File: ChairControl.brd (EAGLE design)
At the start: 150 x 84 mm, 28 parts, among them J1 Digital_0_7, J2 Analog, J3 Digital_8_13, SW1 SWITCH-DPDT3, X1 INPUT, X2 OUTPUT, X4 INPUT

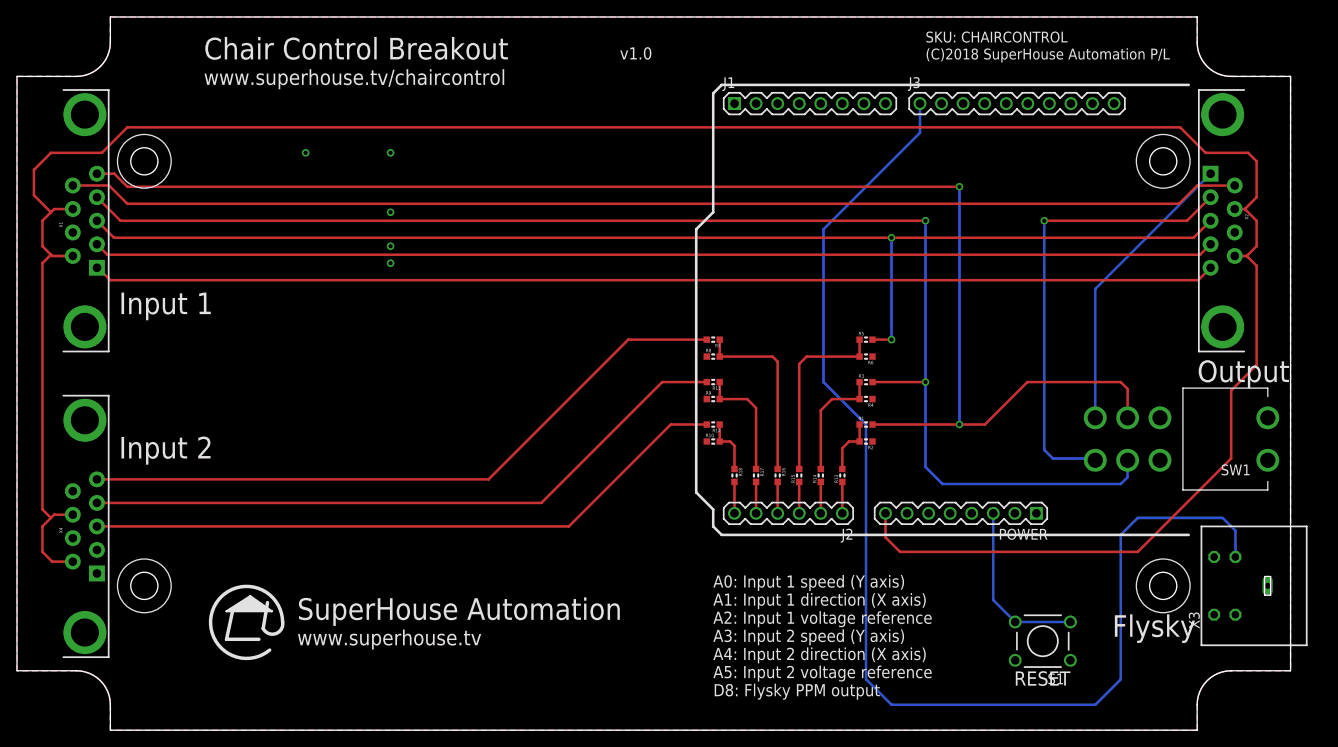
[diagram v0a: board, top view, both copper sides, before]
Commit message: Added trim inputs and extra headers for Mega footprint
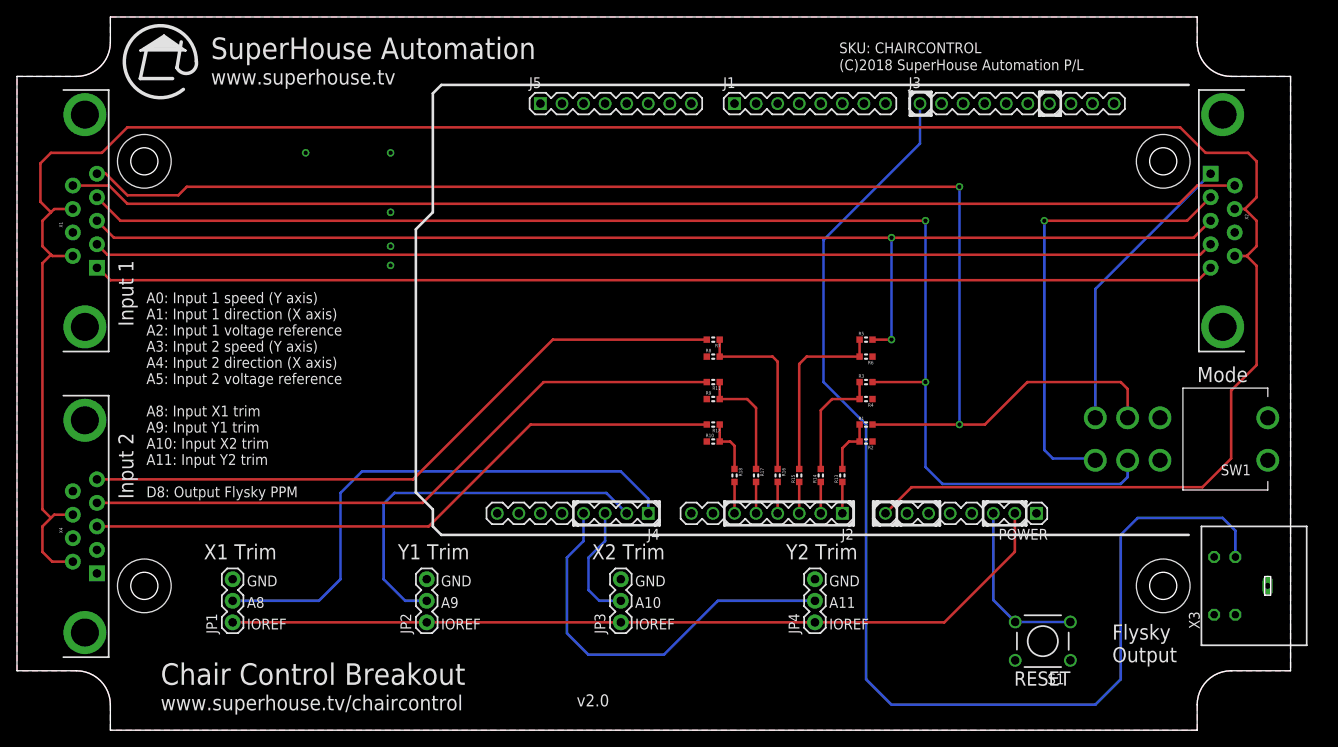
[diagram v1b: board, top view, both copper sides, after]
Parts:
- added J4: Analog, freetronics-jon:1X08
- added J5: Digital_0_7, freetronics:1X08
- added JP1, JP2, JP3, JP4: (no value), freetronics-jon:1X03
- J2: device freetronics:1X06 -> freetronics-jon:1X08
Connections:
- new net A10: J4.3, JP3.2
- new net A11: J4.4, JP4.2
- new net A8: J4.1, JP1.2
- new net A9: J4.2, JP2.2
- net GND: now also JP1.3, JP2.3, JP3.3, JP4.3
- net IOREF: now also JP1.1, JP2.1, JP3.1, JP4.1
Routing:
- net IOREF: track 0.00 -> 100.1 mm
- net A8: track 0.00 -> 64.3 mm
- net A11: track 0.00 -> 47.8 mm
- net A9: track 0.00 -> 45.2 mm
- net A10: track 0.00 -> 14.2 mm
- net 12V: track 297.6 -> 291.5 mm
- net SPEED_IN: track 166.1 -> 166.9 mm
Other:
- board text added: "A0: Input 1 speed (Y axis) A1: Input 1 direction (X axis) A2: Input 1 voltage reference A3: Input 2 speed (Y axis) A4: Input 2 direction (X axis) A5: Input 2 voltage reference A8: Input X1 trim A9: Input Y1 trim A10: Input X2 trim A11: Input Y2 trim D8: Output Flysky PPM"
- board text added: "A10"
- board text added: "A11"
- board text added: "A8"
- board text added: "A9"
- board text added: "Flysky Output"
- board text added: "GND"
- board text added: "IOREF"
- board text added: "Mode"
- board text added: "X1 Trim"
- board text added: "X2 Trim"
- board text added: "Y1 Trim"
- board text added: "Y2 Trim"
- board text added: "v2.0"
- board text removed: "A0: Input 1 speed (Y axis) A1: Input 1 direction (X axis) A2: Input 1 voltage reference A3: Input 2 speed (Y axis) A4: Input 2 direction (X axis) A5: Input 2 voltage reference D8: Flysky PPM output"
- board text removed: "Flysky"
- board text removed: "Output"
- board text removed: "v1.0"
